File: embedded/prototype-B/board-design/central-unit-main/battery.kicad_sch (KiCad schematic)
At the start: 21 parts, among them U3 BQ25887

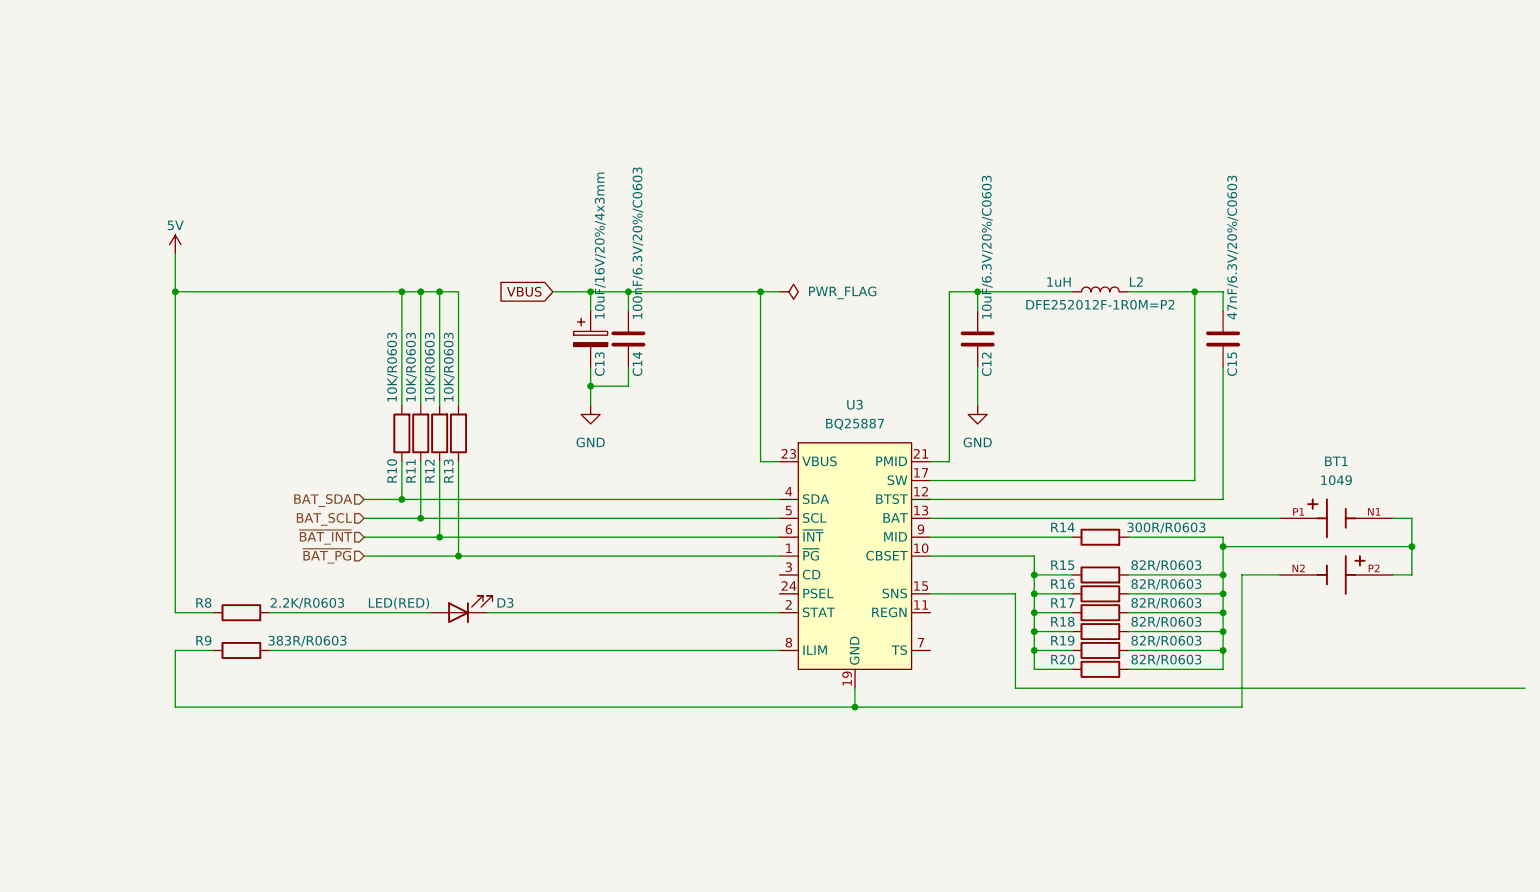
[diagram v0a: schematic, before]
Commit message: [Central Unit] Design USB connection
Schematic of the USB connection and boot considerations for STM32L452RE.

Signed-off-by: Nicolae-Andrei Vasile <vasilenicolaeandrei@gmail.com>
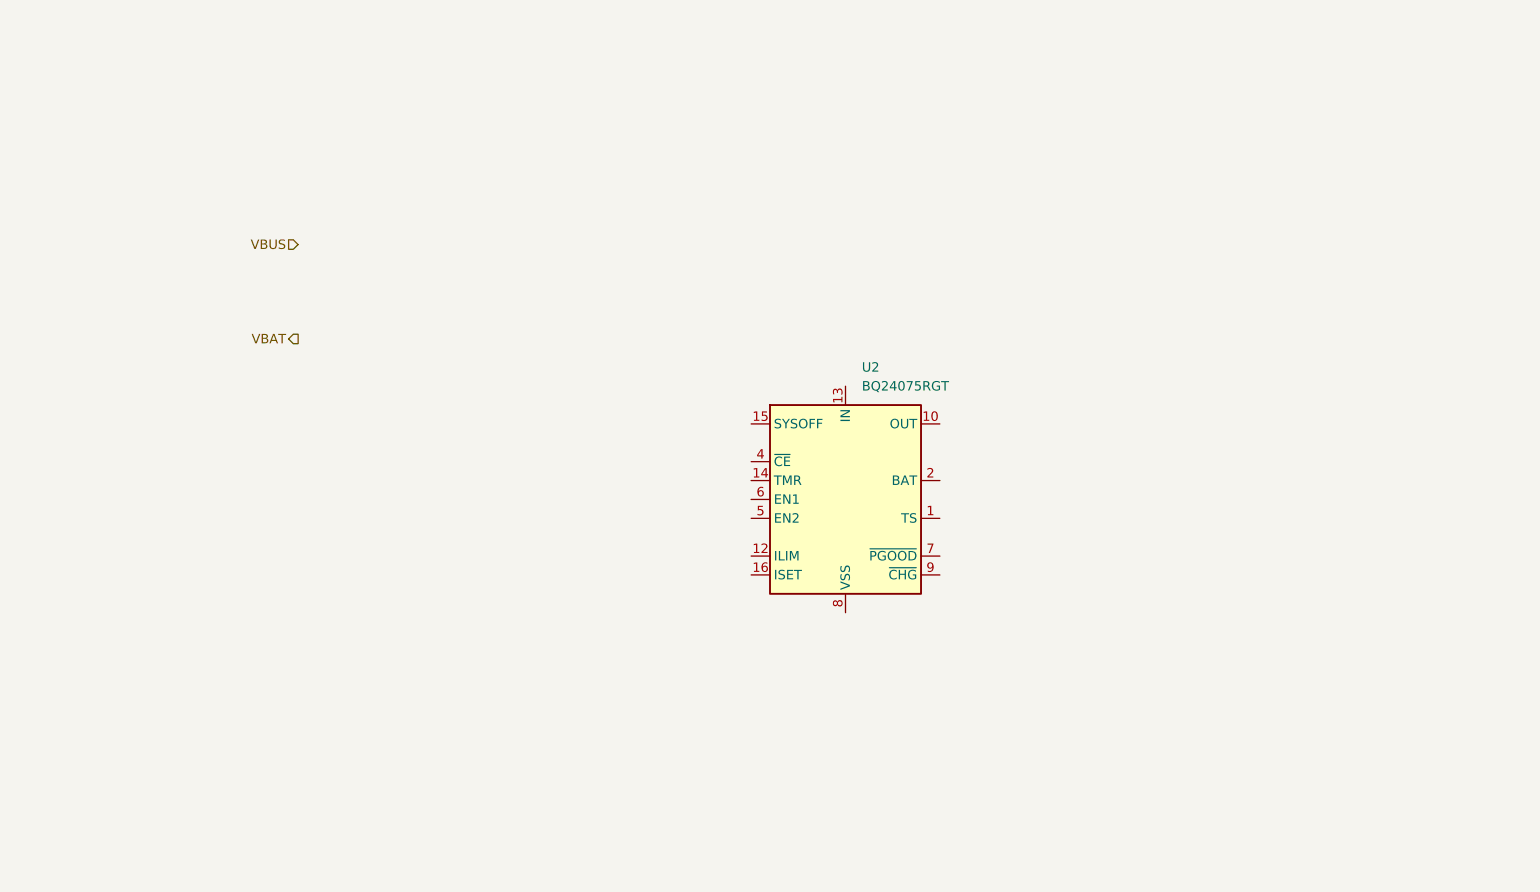
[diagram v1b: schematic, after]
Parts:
- removed BT1: 1049, 1049:BAT_1049, symbol 1049:1049
- removed C12: 10uF/6.3V/20%/C0603, Capacitor_SMD:C_0603_1608Metric_Pad1.08x0.95mm_HandSolder, symbol Device:C
- removed C13: 10uF/16V/20%/4x3mm, Capacitor_SMD:CP_Elec_4x3, symbol Device:C_Polarized
- removed C14: 100nF/6.3V/20%/C0603, Capacitor_SMD:C_0603_1608Metric_Pad1.08x0.95mm_HandSolder, symbol Device:C
- removed C15: 47nF/6.3V/20%/C0603, Capacitor_SMD:C_0603_1608Metric_Pad1.08x0.95mm_HandSolder, symbol Device:C
- removed D3: LED(RED), LED_SMD:LED_0603_1608Metric_Pad1.05x0.95mm_HandSolder, symbol Device:LED
- removed L2: 1uH, Inductor_SMD:L_1210_3225Metric_Pad1.42x2.65mm_HandSolder, symbol SparkFun-Coil:L
- removed R10, R11, R12, R13: 10K/R0603, Resistor_SMD:R_0603_1608Metric_Pad0.98x0.95mm_HandSolder, symbol Device:R
- removed R14: 300R/R0603, Resistor_SMD:R_0603_1608Metric_Pad0.98x0.95mm_HandSolder, symbol Device:R
- removed R15, R16, R17, R18, R19, R20: 82R/R0603, Resistor_SMD:R_0603_1608Metric_Pad0.98x0.95mm_HandSolder, symbol Device:R
- removed R8: 2.2K/R0603, Resistor_SMD:R_0603_1608Metric_Pad0.98x0.95mm_HandSolder, symbol Device:R
- removed R9: 383R/R0603, Resistor_SMD:R_0603_1608Metric_Pad0.98x0.95mm_HandSolder, symbol Device:R
- removed U3: BQ25887, Package_DFN_QFN:VQFN-24-1EP_4x4mm_P0.5mm_EP2.5x2.5mm, symbol Battery_Management:BQ25887
- added U2: BQ24075RGT, Package_DFN_QFN:VQFN-16-1EP_3x3mm_P0.5mm_EP1.6x1.6mm, symbol Battery_Management:BQ24075RGT
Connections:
- new net: U2.10 (OUT), U2.11 (OUT)
- new net: U2.17 (VSS), U2.8 (VSS)
- new net: U2.2 (BAT), U2.3 (BAT)

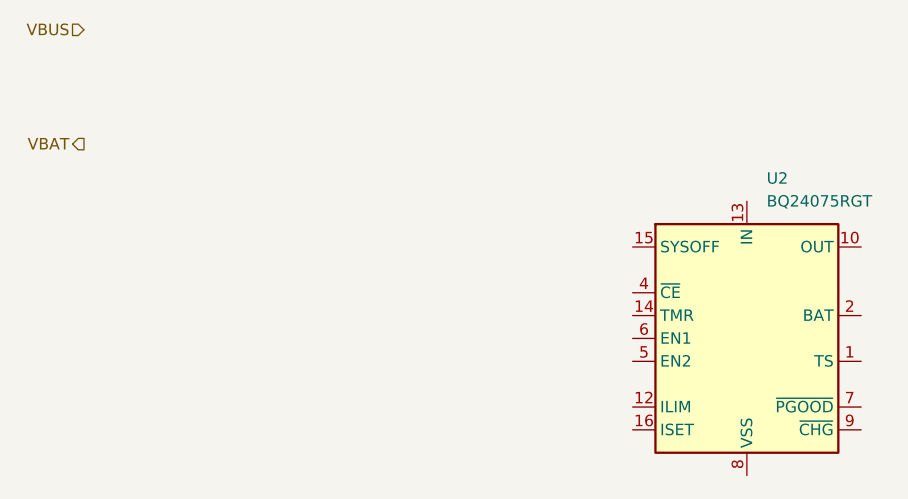
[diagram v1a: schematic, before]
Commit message: [Central unit] Power domain
Documented and implemented a first version of the main power domain for
the device.

Signed-off-by: Nicolae-Andrei Vasile <vasilenicolaeandrei@gmail.com>
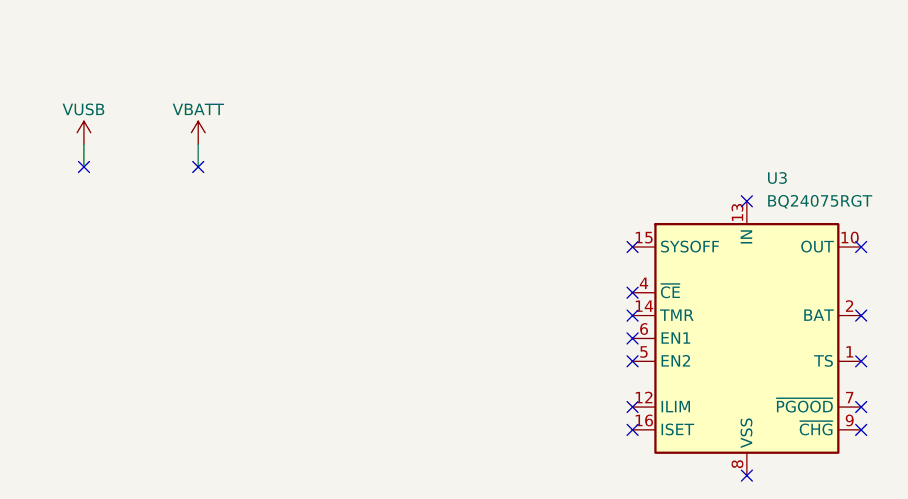
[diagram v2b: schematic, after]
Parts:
- renumbered U2 to U3
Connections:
- no-connect marks 0 -> 16
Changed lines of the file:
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@@
 	(generator_version "8.0")
 	(paper "A4")
-	(hierarchical_label "VBAT"
-		(shape output)
-		(at 63.5 63.5 180)
-		(effects
-			(font
-				(size 1.27 1.27)
-			)
-			(justify right)
-		)
-	)
-	(hierarchical_label "VBUS"
-		(shape input)
-		(at 63.5 50.8 180)
-		(effects
-			(font
-				(size 1.27 1.27)
-			)
-			(justify right)
+	(no_connect
+		(at 149.86 87.63)
+	)
+	(no_connect
+		(at 76.2 66.04)
+	)
+	(no_connect
+		(at 149.86 92.71)
+	)
+	(no_connect
+		(at 124.46 74.93)
+	)
+	(no_connect
+		(at 63.5 66.04)
+	)
+	(no_connect
+		(at 149.86 74.93)
+	)
+	(no_connect
+		(at 149.86 95.25)
+	)
+	(no_connect
+		(at 124.46 82.55)
+	)
+	(no_connect
+		(at 124.46 85.09)
+	)
+	(no_connect
+		(at 124.46 95.25)
+	)
+	(no_connect
+		(at 124.46 80.01)
+	)
+	(no_connect
+		(at 137.16 100.33)
+	)
+	(no_connect
+		(at 124.46 92.71)
+	)
+	(no_connect
+		(at 149.86 82.55)
+	)
+	(no_connect
+		(at 137.16 69.85)
+	)
+	(no_connect
+		(at 124.46 87.63)
+	)
+	(wire
+		(pts
+			(xy 76.2 63.5) (xy 76.2 66.04)
+		)
+		(stroke
+			(width 0)
+			(type default)
+		)
+	)
+	(wire
+		(pts
+			(xy 63.5 63.5) (xy 63.5 66.04)
+		)
+		(stroke
+			(width 0)
+			(type default)
+		)
+	)
+	(symbol
+		(lib_id "SparkFun-PowerSymbol:VUSB")
+		(at 63.5 63.5 0)
+		(unit 1)
+		(exclude_from_sim no)
+		(in_bom yes)
+		(on_board yes)
+		(dnp no)
+		(fields_autoplaced yes)
+		(property "Reference" "#PWR25"
+			(at 63.5 67.31 0)
+			(effects
+				(font
+					(size 1.27 1.27)
+				)
+				(hide yes)
+			)
+		)
+		(property "Value" "VUSB"
+			(at 63.5 59.69 0)
+			(do_not_autoplace yes)
+			(effects
+				(font
+					(size 1.27 1.27)
+				)
+			)
+		)
+		(property "Footprint" ""
+			(at 63.5 63.5 0)
+			(effects
+				(font
+					(size 1.27 1.27)
+				)
+				(hide yes)
+			)
+		)
+		(property "Datasheet" ""
+			(at 63.5 63.5 0)
+			(effects
+				(font
+					(size 1.27 1.27)
+				)
+				(hide yes)
+			)
+		)
+		(property "Description" "Power symbol creates a global label with name \"VUSB\""
+			(at 63.5 69.85 0)
+			(effects
+				(font
+					(size 1.27 1.27)
+				)
+				(hide yes)
+			)
+		)
+		(pin "1"
+		)
+		(instances
+			(project ""
+				(path "/baa8ab85-8b75-4cee-ab91-40606360b161/0d9b0fcc-d01e-4009-b64e-b7ee43f093f4"
+					(reference "#PWR25")
+					(unit 1)
+				)
+			)
 		)
 	)
@@
 		(dnp no)
 		(fields_autoplaced yes)
-		(property "Reference" "U2"
+		(property "Reference" "U3"
 			(at 139.3541 67.31 0)
 			(effects
@@
 			(project ""
 				(path "/baa8ab85-8b75-4cee-ab91-40606360b161/0d9b0fcc-d01e-4009-b64e-b7ee43f093f4"
-					(reference "U2")
+					(reference "U3")
 					(unit 1)
 				)
+			)
+		)
+	)
+	(symbol
+		(lib_id "SparkFun-PowerSymbol:VBATT")
+		(at 76.2 63.5 0)
+		(unit 1)
+		(exclude_from_sim no)
+		(in_bom yes)
+		(on_board yes)
+		(dnp no)
+		(fields_autoplaced yes)
+		(property "Reference" "#PWR26"
+			(at 76.2 67.31 0)
+			(effects
+				(font
+					(size 1.27 1.27)
+				)
+				(hide yes)
+			)
+		)
+		(property "Value" "VBATT"
+			(at 76.2 59.69 0)
+			(do_not_autoplace yes)
+			(effects
+				(font
+					(size 1.27 1.27)
+				)
+			)
+		)
+		(property "Footprint" ""
+			(at 76.2 63.5 0)
+			(effects
+				(font
+					(size 1.27 1.27)
+				)
+				(hide yes)
+			)
+		)
+		(property "Datasheet" ""
+			(at 76.2 63.5 0)
+			(effects
+				(font
+					(size 1.27 1.27)
+				)
+				(hide yes)
+			)
+		)
+		(property "Description" "Power symbol creates a global label with name \"VBATT\""
+			(at 76.2 69.85 0)
+			(effects
+				(font
+					(size 1.27 1.27)
+				)
+				(hide yes)
+			)
+		)
+		(pin "1"
+		)
+		(instances
+			(project ""
+				(path "/baa8ab85-8b75-4cee-ab91-40606360b161/0d9b0fcc-d01e-4009-b64e-b7ee43f093f4"
+					(reference "#PWR26")
+					(unit 1)
+				)

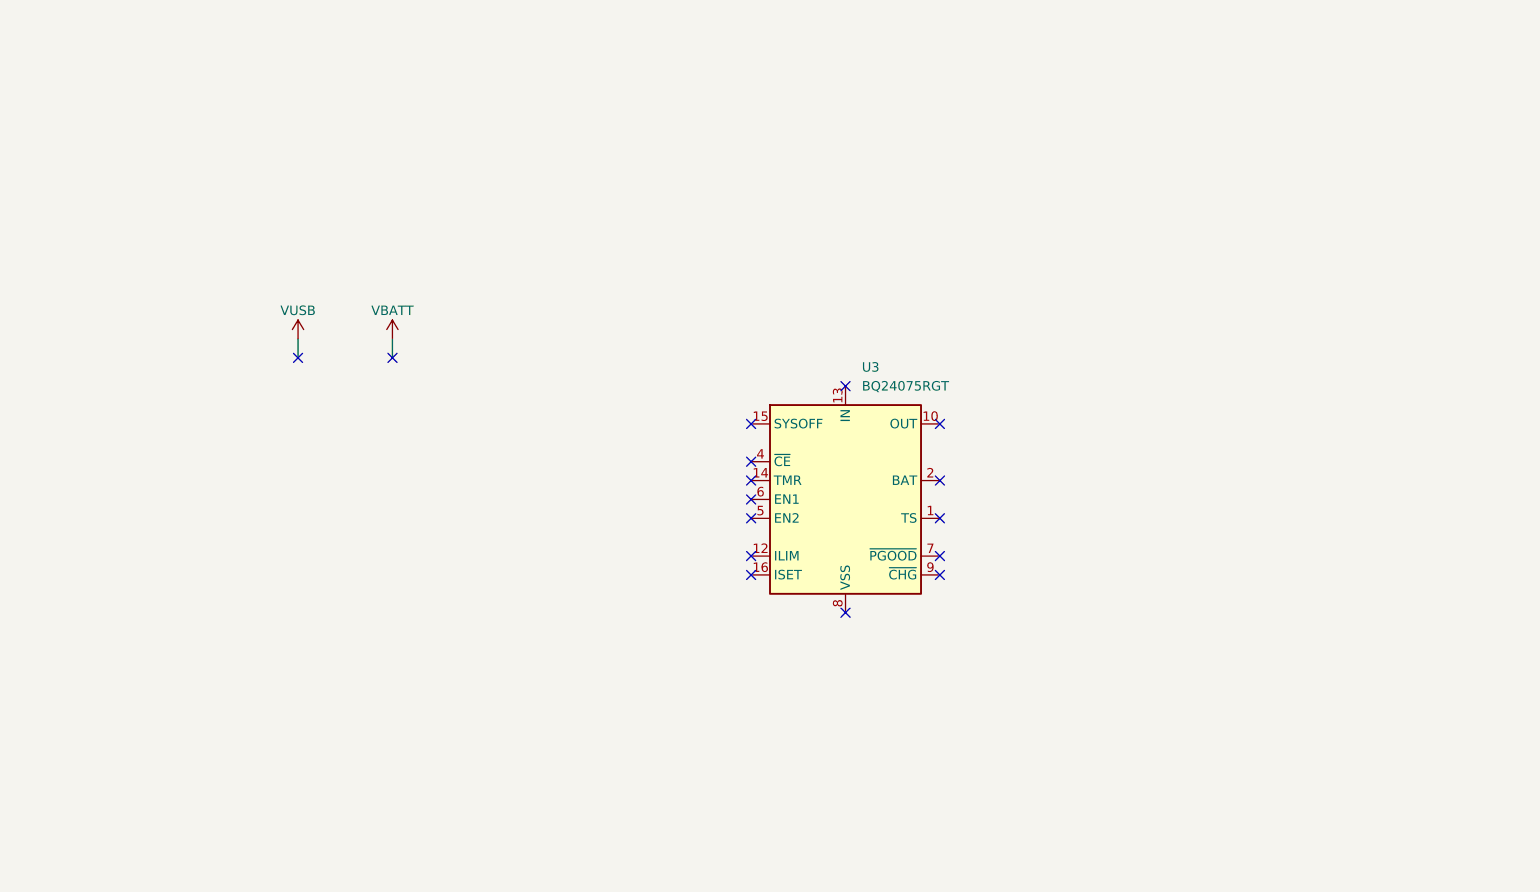
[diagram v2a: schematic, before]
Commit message: [Central unit] Battery charger
Added battery charging circuit to the schematic. Refactored BOOT0 logic
and included an entry for the external push button to power ON/OFF the device.

Signed-off-by: Nicolae-Andrei Vasile <vasilenicolaeandrei@gmail.com>
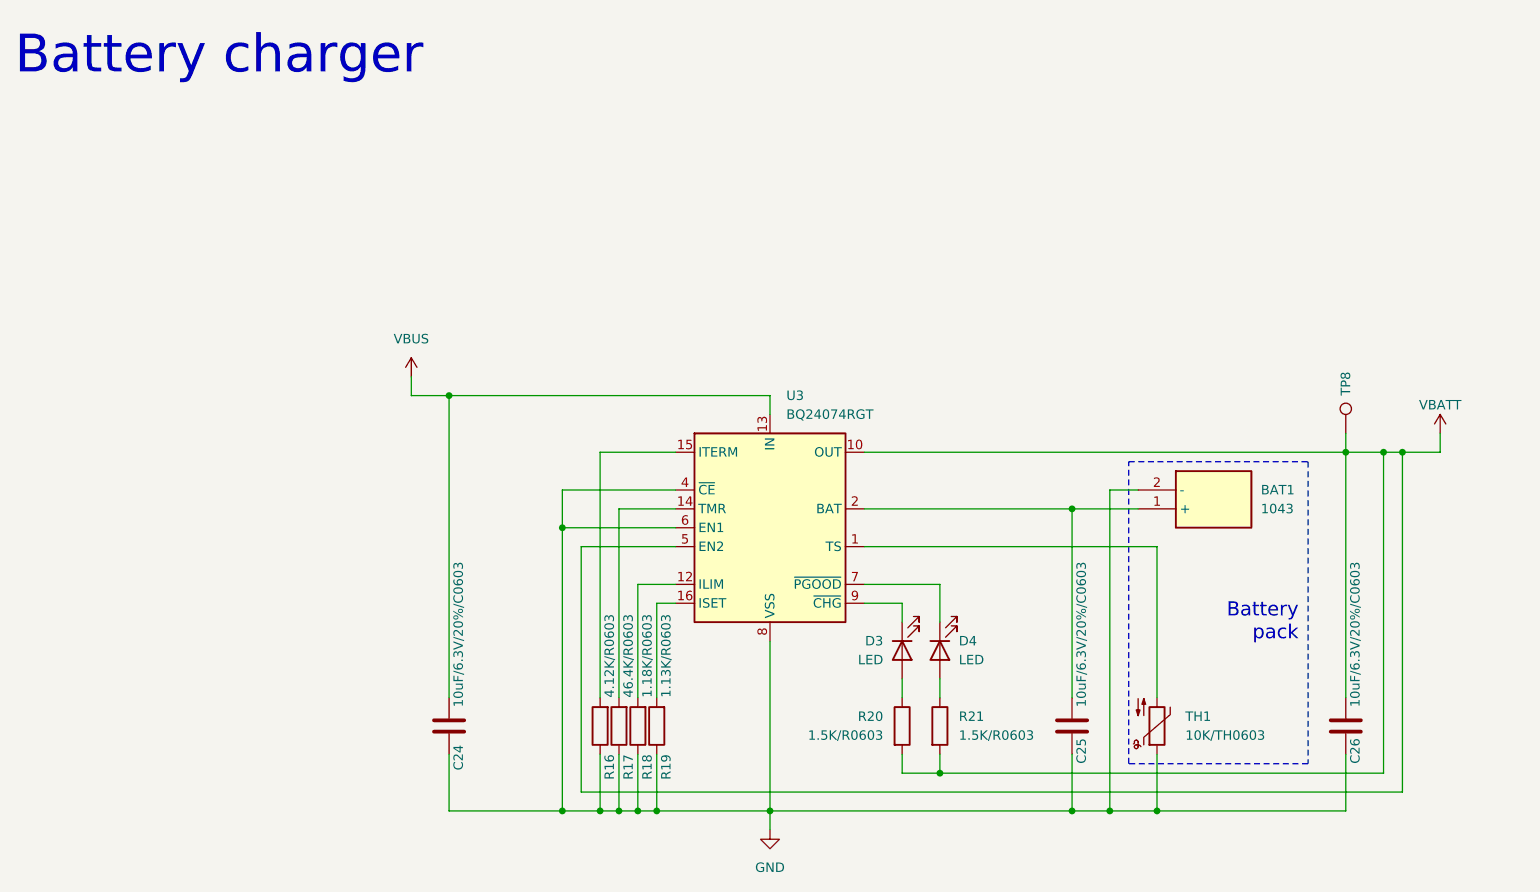
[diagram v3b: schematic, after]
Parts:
- removed U3: BQ24075RGT, Package_DFN_QFN:VQFN-16-1EP_3x3mm_P0.5mm_EP1.6x1.6mm, symbol Battery_Management:BQ24075RGT
- added BAT1: 1043, 1043:1043, symbol 1043:1043
- added C24, C25, C26: 10uF/6.3V/20%/C0603, Capacitor_SMD:C_0603_1608Metric_Pad1.08x0.95mm_HandSolder, symbol Device:C
- added D3, D4: LED, LED_SMD:LED_0805_2012Metric_Pad1.15x1.40mm_HandSolder, symbol Device:LED
- added R16: 4.12K/R0603, Resistor_SMD:R_0603_1608Metric_Pad0.98x0.95mm_HandSolder, symbol Device:R
- added R17: 46.4K/R0603, Resistor_SMD:R_0603_1608Metric_Pad0.98x0.95mm_HandSolder, symbol Device:R
- added R18: 1.18K/R0603, Resistor_SMD:R_0603_1608Metric_Pad0.98x0.95mm_HandSolder, symbol Device:R
- added R19: 1.13K/R0603, Resistor_SMD:R_0603_1608Metric_Pad0.98x0.95mm_HandSolder, symbol Device:R
- added R20, R21: 1.5K/R0603, Resistor_SMD:R_0603_1608Metric_Pad0.98x0.95mm_HandSolder, symbol Device:R
- added TH1: 10K/TH0603, Resistor_SMD:R_0603_1608Metric_Pad0.98x0.95mm_HandSolder, symbol Device:Thermistor_NTC
- added TP8: TestPoint, symbol Connector:TestPoint
- added U3: BQ24074RGT, Package_DFN_QFN:VQFN-16-1EP_3x3mm_P0.5mm_EP1.6x1.6mm, symbol Battery_Management:BQ24074RGT
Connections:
- net VBATT: now also C26.1, R20.2, R21.2, TP8.1, U3.10 (OUT), U3.11 (OUT), U3.5 (EN2)
- new net: BAT1.1 (+), C25.1, U3.2 (BAT), U3.3 (BAT)
- new net: D3.1 (K), U3.9 (~{CHG})
- new net: D3.2 (A), R20.1
- new net: D4.1 (K), U3.7 (~{PGOOD})
- new net: D4.2 (A), R21.1
- new net: R17.2, U3.14 (TMR)
- new net: R18.2, U3.12 (ILIM)
- new net: R16.2, U3.15 (ITERM)
- new net: TH1.2, U3.1 (TS)
- new net: R19.2, U3.16 (ISET)
- new net GND: BAT1.2 (-), C24.2, C25.2, C26.2, R16.1, R17.1, R18.1, R19.1, TH1.1, U3.17 (VSS), U3.4 (~{CE}), U3.6 (EN1), U3.8 (VSS)
- new net VBUS: C24.1, U3.13 (IN)
- no-connect marks 16 -> 0
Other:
- note added: "Battery charger"
- note added: "Battery pack"
- title: (none) -> Retrolight
